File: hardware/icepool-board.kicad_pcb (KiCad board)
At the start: 4 copper layers, 66 x 58 mm, 184 parts, among them J1 USB Micro, J2 PWR_IN, J3 SWD, J4 I2C, J5 RS485, SW1 B3U-1000P, U1 ATSAMD21E, U2 ISL83485, U3 iCE40HX8K-BG121(121-Ball_caBG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, U4 iCE40HX8K-BG121(121-Ball_caBG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, U5 iCE40HX8K-BG121(121-Ball_caBG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, U6 iCE40HX8K-BG121(121-Ball_caBG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, U7 FAN2306, U8 TPS715_SC70, U9 FAN2306, X1 CB3LV-3I-16M0000, X2 CB3LV-3I-16M0000, X3 CB3LV-3I-16M0000, X4 CB3LV-3I-16M0000, Y1 16MHz

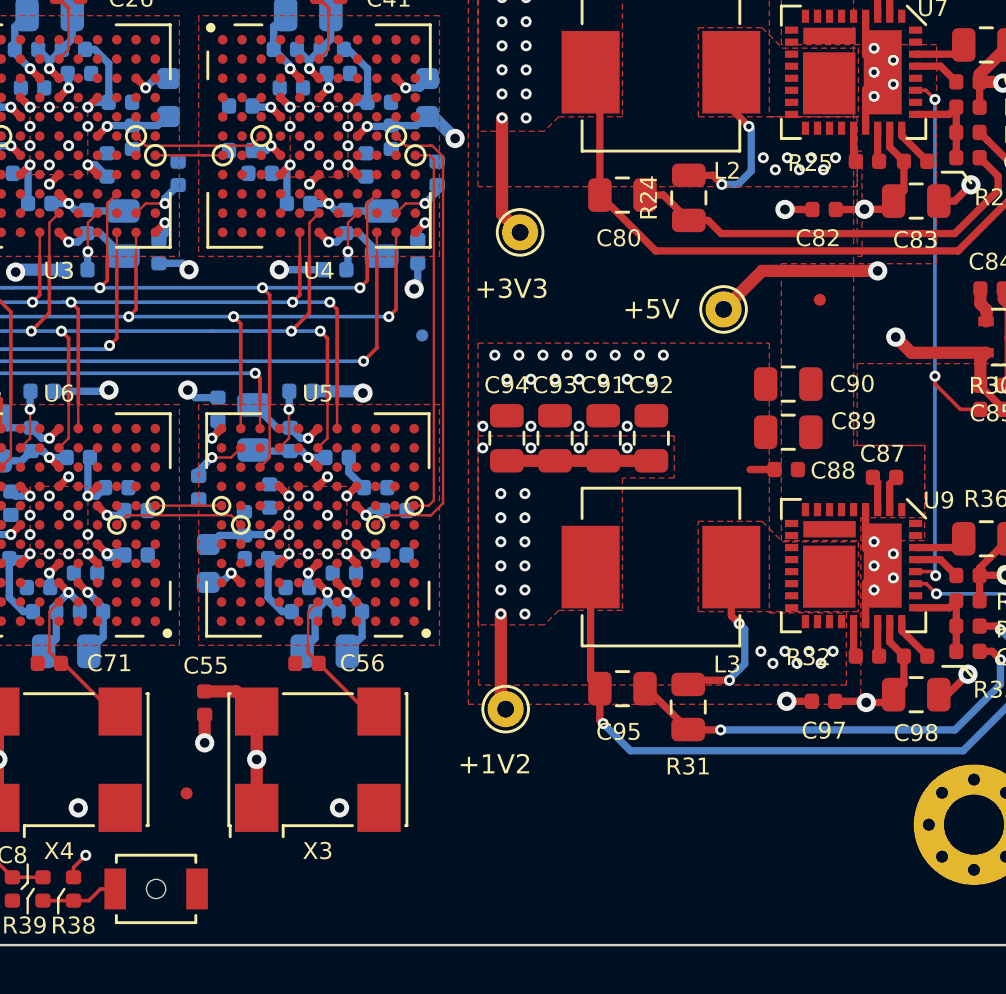
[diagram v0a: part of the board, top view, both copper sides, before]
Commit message: Added OSHW logo. Ready to order 2020-01.
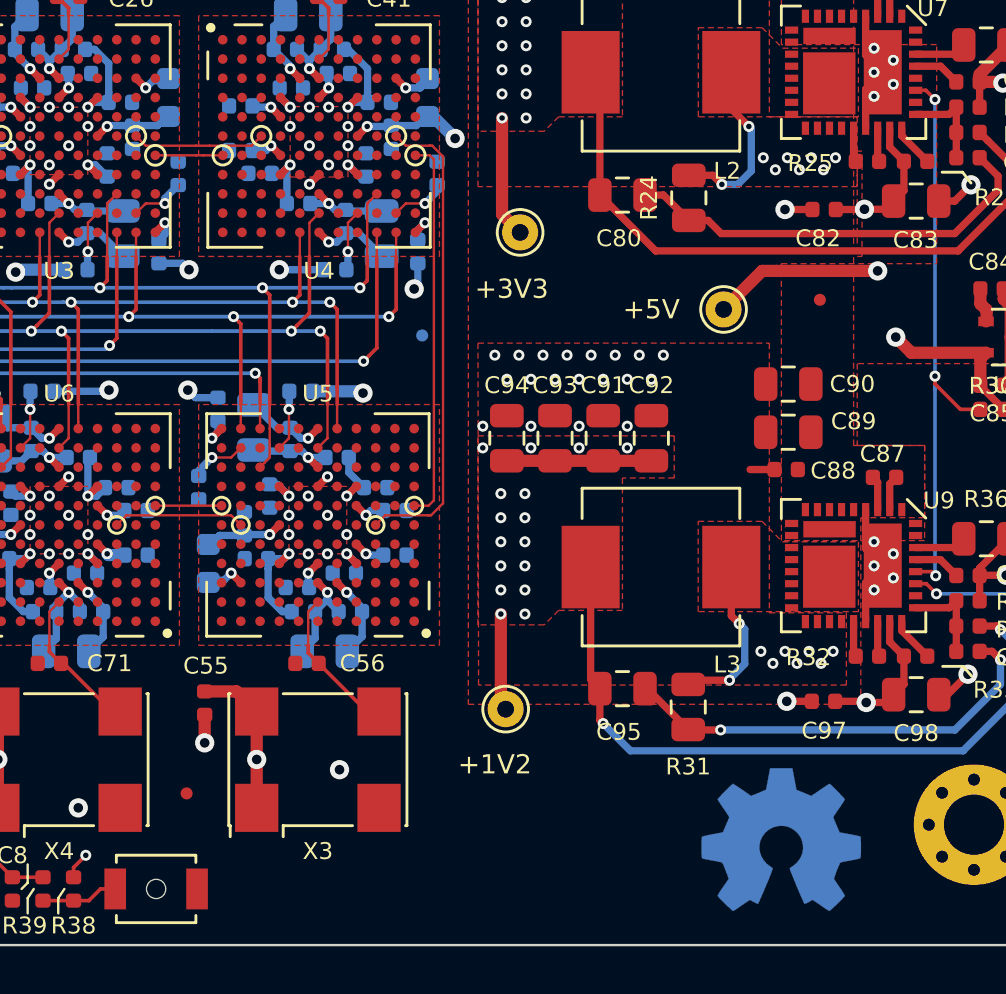
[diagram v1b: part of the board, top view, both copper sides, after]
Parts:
- added REF**: OSHW-Symbol_6.7x6mm_Copper, Symbol:OSHW-Symbol_6.7x6mm_Copper, B.Cu at (163.0, 135.6)

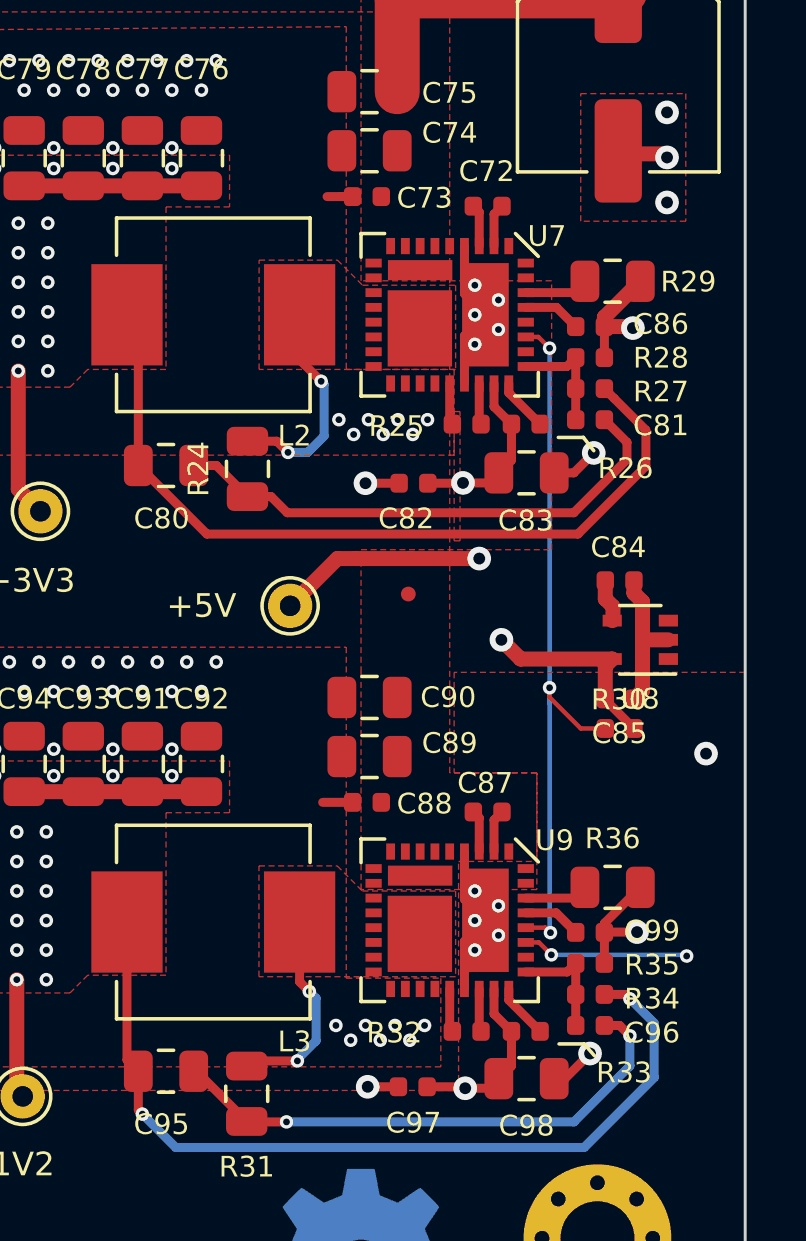
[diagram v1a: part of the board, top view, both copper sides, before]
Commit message: Fixed 3v3 and 1v2 buck component values.
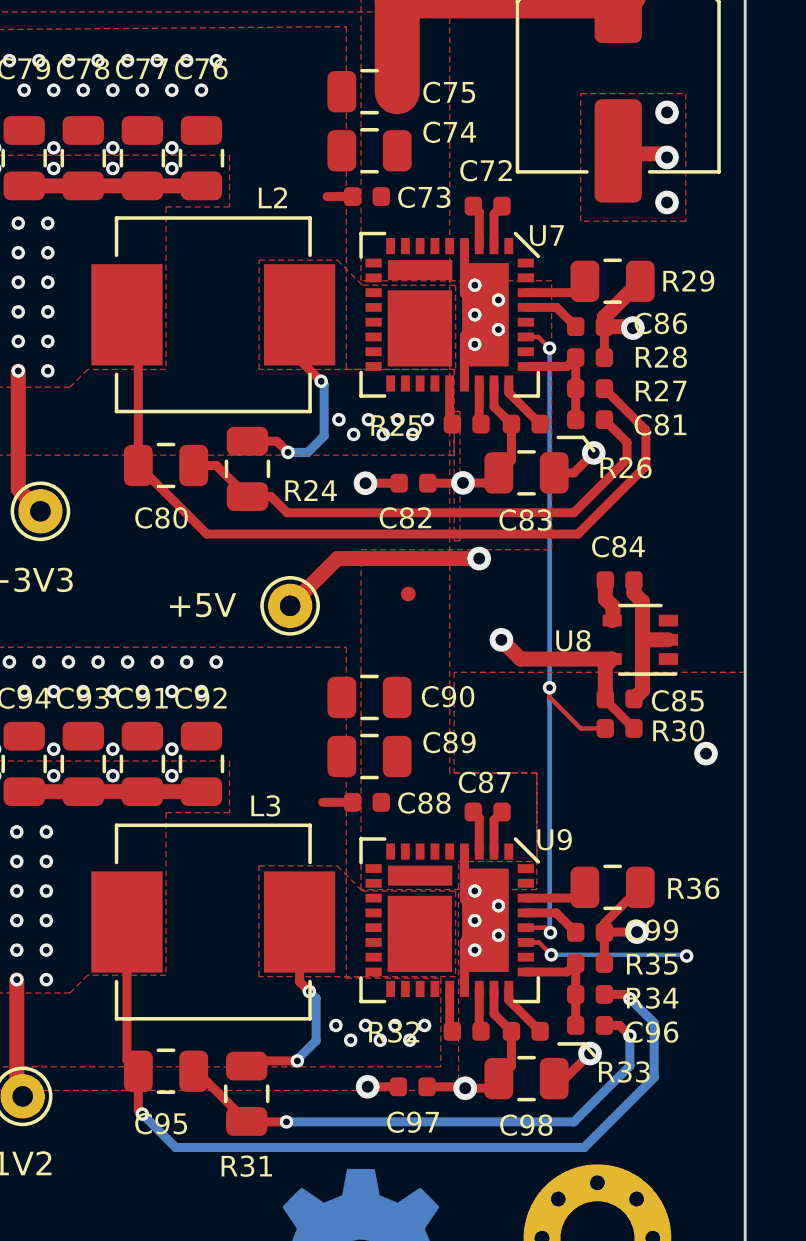
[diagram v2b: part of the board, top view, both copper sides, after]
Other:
- board text added: "icepool-board 2020-02 fourside.io"
- board text removed: "icepool-board 2020-01 fourside.io"
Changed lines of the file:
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@@
     (tags resistor)
     (attr smd)
-    (fp_text reference R24 (at 0 -1.65 90) (layer F.SilkS)
+    (fp_text reference R24 (at -0.762 2.1336 180) (layer F.SilkS)
       (effects (font (size 0.7 0.7) (thickness 0.1)))
     )
@@
     (tags resistor)
     (attr smd)
-    (fp_text reference R36 (at 0 -1.65) (layer F.SilkS)
+    (fp_text reference R36 (at 2.7305 0.0635) (layer F.SilkS)
       (effects (font (size 0.7 0.7) (thickness 0.1)))
     )
@@
     (tags "SOT-353 SC-70-5")
     (attr smd)
-    (fp_text reference U8 (at 0 -2) (layer F.SilkS)
+    (fp_text reference U8 (at 2.27 -0.058) (layer F.SilkS)
       (effects (font (size 0.7 0.7) (thickness 0.1)))
     )
@@
     (tags capacitor)
     (attr smd)
-    (fp_text reference C85 (at 0 -1.17) (layer F.SilkS)
+    (fp_text reference C85 (at -1.986 -0.09) (layer F.SilkS)
       (effects (font (size 0.7 0.7) (thickness 0.1)))
     )
@@
     (tags "inductor vishay ihlp smd")
     (attr smd)
-    (fp_text reference L3 (at -2.75 -4.05) (layer F.SilkS)
+    (fp_text reference L3 (at -1.766 3.904) (layer F.SilkS)
       (effects (font (size 0.7 0.7) (thickness 0.1)))
     )
@@
     (tags "inductor vishay ihlp smd")
     (attr smd)
-    (fp_text reference L2 (at -2.75 -4.1) (layer F.SilkS)
+    (fp_text reference L2 (at -2.02 3.928) (layer F.SilkS)
       (effects (font (size 0.7 0.7) (thickness 0.1)))
     )
@@
     (tags resistor)
     (attr smd)
-    (fp_text reference R30 (at 0.025 0.975) (layer F.SilkS)
+    (fp_text reference R30 (at -1.986 -0.106) (layer F.SilkS)
       (effects (font (size 0.7 0.7) (thickness 0.1)))
     )
@@
     (effects (font (size 0.8 0.8) (thickness 0.1)))
   )
-  (gr_text "icepool-board 2020-01\nfourside.io" (at 158.5595 135.636) (layer B.Mask)
+  (gr_text "icepool-board 2020-02\nfourside.io" (at 158.5595 135.636) (layer B.Mask)
     (effects (font (size 1 1) (thickness 0.2)) (justify left mirror))
   )

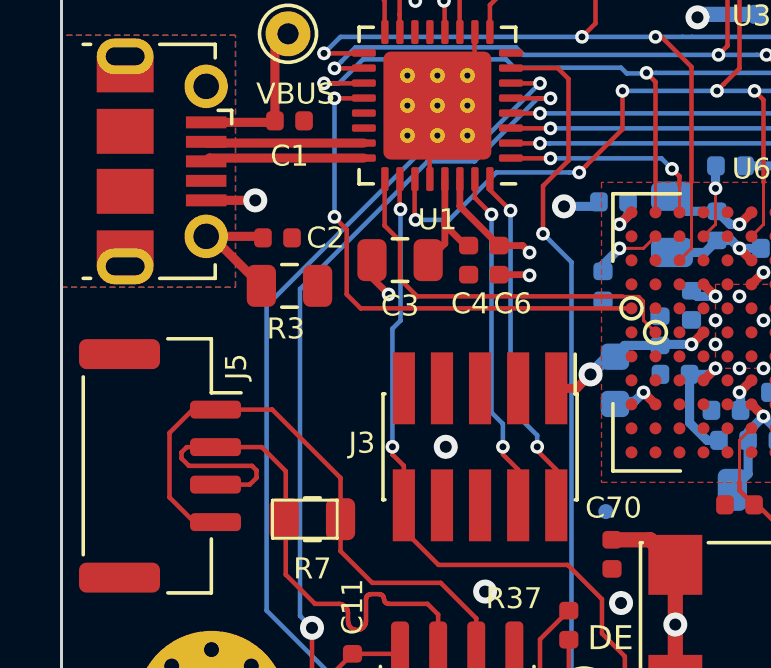
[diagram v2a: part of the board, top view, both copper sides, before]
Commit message: Changed MCU crystal to 2.5x2mm @ 16MHz. Resolves #20
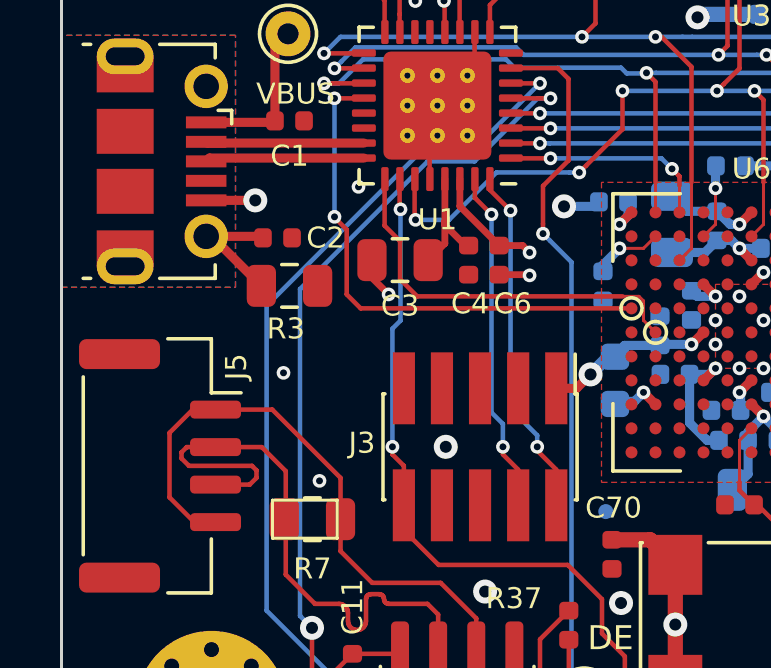
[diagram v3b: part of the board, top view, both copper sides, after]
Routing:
- net GND: vias 121 -> 124
- removed copper zone on F.Cu, net (none)
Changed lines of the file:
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@@
     (thickness 1.6)
     (drawings 59)
-    (tracks 1398)
+    (tracks 1401)
     (zones 0)
     (modules 185)
@@
   (gr_line (start 112.5 140) (end 173.5 140) (layer Edge.Cuts) (width 0.1))
   (gr_line (start 110 84.5) (end 110 137.5) (layer Edge.Cuts) (width 0.1))
+  (via (at 118.6 127.5) (size 0.4572) (drill 0.2286) (layers F.Cu B.Cu) (net 1))
   (via (at 173.355 96.901) (size 0.8) (drill 0.4) (layers F.Cu B.Cu) (net 1))
   (via (at 166.85 102.75) (size 0.4572) (drill 0.2286) (layers F.Cu B.Cu) (net 1))
@@
   (segment (start 125.58 120.627) (end 125.603 120.65) (width 0.2286) (layer F.Cu) (net 1))
   (segment (start 124.587 120.627) (end 125.58 120.627) (width 0.2286) (layer F.Cu) (net 1))
+  (via (at 117.4 123.9) (size 0.4572) (drill 0.2286) (layers F.Cu B.Cu) (net 1))
+  (via (at 119.9 117.7) (size 0.4572) (drill 0.2286) (layers F.Cu B.Cu) (net 1))
   (segment (start 171.525 114.075) (end 171.5 114.1) (width 0.508) (layer F.Cu) (net 2))
   (segment (start 171.525 113.625) (end 171.525 114.075) (width 0.508) (layer F.Cu) (net 2))
@@
     )
   )
-  (zone (net 0) (net_name "") (layer F.Cu) (hatch edge 0.508)
+  (zone (net 1) (net_name GND) (layer F.Cu) (hatch edge 0.508)
     (priority 7)
     (connect_pads (clearance 0.1016))
